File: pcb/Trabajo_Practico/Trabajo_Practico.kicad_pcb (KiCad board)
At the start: 2 copper layers, 72.5 x 56 mm, 13 parts, among them J1 Conn_02x19_Odd_Even, J2 Conn_02x19_Odd_Even, J3 Conn_01x03_Male, J4 Conn_01x03_Male, U1 ESP8266-01_ESP-01, U2 MAX30102_P, U3 SD_Card_P, U4 DS18B20

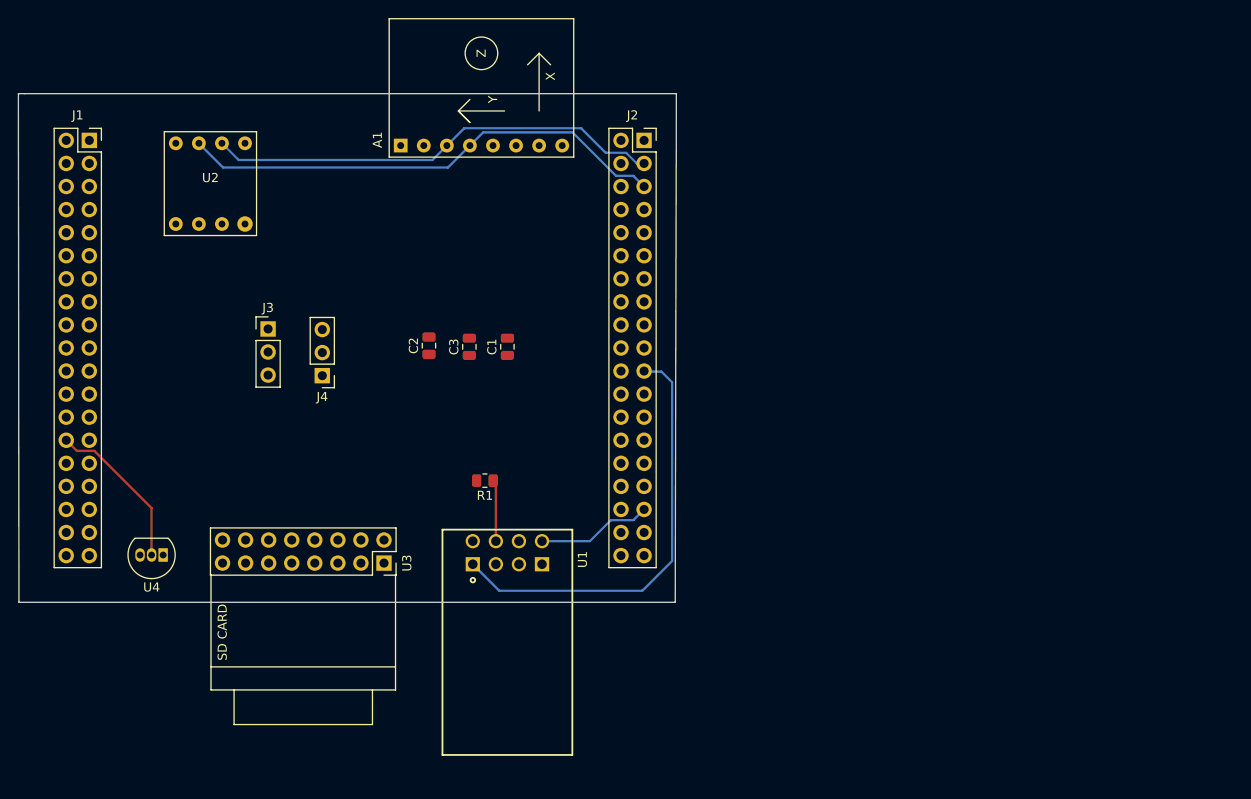
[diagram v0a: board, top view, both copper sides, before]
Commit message: Se ordena los componentes en el pcb
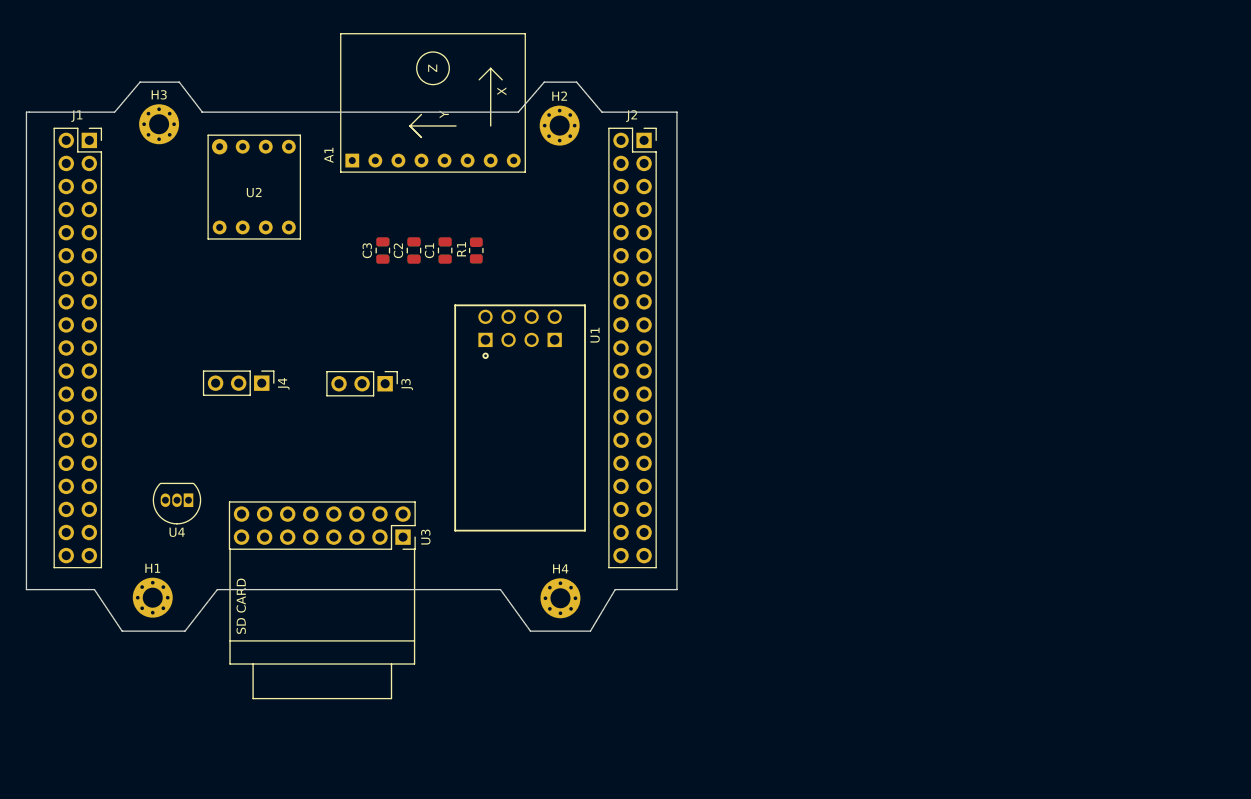
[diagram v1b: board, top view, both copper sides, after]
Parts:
- added H1: MountingHole, MountingHole:MountingHole_2.2mm_M2_Pad_Via, F.Cu at (53.4, 102.5)
- added H2: MountingHole, MountingHole:MountingHole_2.2mm_M2_Pad_Via, F.Cu at (98.2, 50.5)
- added H3: MountingHole, MountingHole:MountingHole_2.2mm_M2_Pad_Via, F.Cu at (54.1, 50.4)
- added H4: MountingHole, MountingHole:MountingHole_2.2mm_M2_Pad_Via, F.Cu at (98.3, 102.6)
- moved R1 25.4 mm to (89.0, 64.3), turned to 270 degrees
- moved U1 24.7 mm to (93.9, 74.1)
- moved C3 14.3 mm to (78.7, 64.3)
- moved J3 14.2 mm to (79.0, 78.9), turned to 270 degrees
- moved C1 12.6 mm to (85.6, 64.3)
- moved C2 10.6 mm to (82.2, 64.3)
- moved U2 8.81 mm to (63.3, 52.8), turned to 0 degrees
- moved J4 6.72 mm to (65.4, 78.9), turned to 270 degrees
- moved U4 6.65 mm to (57.3, 91.8)
- moved A1 5.58 mm to (75.4, 54.4)
- moved U3 3.54 mm to (81.0, 95.8)
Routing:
- net /PB9: track 54.2 -> 0.00 mm
- net /PB8: track 50.3 -> 0.00 mm
- net /PA9: track 47.8 -> 0.09 mm
- net /AN0: track 17.7 -> 0.00 mm
- net /PA10: track 12.7 -> 0.00 mm
- net Net-(R1-Pad1): track 6.79 -> 0.00 mm
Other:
- board size 72.5 x 56 mm -> 71.6 x 60.5 mm

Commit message: Se realizaron las correcciones
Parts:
- U4: footprint Package_TO_SOT_THT:TO-92_Inline -> Connector_PinHeader_2.54mm:PinHeader_1x03_P2.54mm_Vertical
- moved R1 37.9 mm to (54.0, 78.7), turned to 0 degrees
- moved C2 34.5 mm to (54.2, 84.5), turned to 180 degrees
- moved C1 30.1 mm to (59.2, 78.7), turned to 0 degrees
- moved C3 28.0 mm to (59.3, 84.5), turned to 0 degrees
- moved J3 26.3 mm to (99.6, 95.2)
- moved U4 18.8 mm to (72.2, 80.2), turned to 90 degrees
- moved J4 17.7 mm to (58.7, 95.2)
- moved A1 15.4 mm to (65.9, 66.5)
- moved U2 10.6 mm to (55.6, 60.0)
- moved J5 4.02 mm to (84.3, 93.5)
- moved U1 3.30 mm to (93.8, 77.4), turned to 90 degrees
- renumbered U3 to J5
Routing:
- net VCC: track 0.00 -> 110.6 mm
- net /PB8: track 0.00 -> 61.0 mm
- net /PB9: track 0.00 -> 57.6 mm
- net /CLK: track 0.00 -> 44.6 mm
- net Net-(R1-Pad1): track 0.00 -> 44.5 mm
- net /CS: track 0.00 -> 40.6 mm
- net /MOSI: track 0.00 -> 33.9 mm
- net /MISO: track 0.00 -> 33.0 mm
- net /AN0: track 0.00 -> 32.9 mm
- net /PA10: track 0.00 -> 31.4 mm
- net /PA9: track 0.09 -> 11.2 mm
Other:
- outline, holes or cut-outs redrawn
- rule via_min_drill: 0.3 -> 0.4
- rule via_min_size: 0.4 -> 0.5

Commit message: Presentacion final del proyecto
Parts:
- added C4: 100nF, Capacitor_SMD:C_0805_2012Metric, F.Cu at (116.3, 83.2)
- added D1: LED, LED_SMD:LED_0805_2012Metric_Pad1.15x1.40mm_HandSolder, F.Cu at (160.3, 101.0)
- added FID1: Fiducial, Fiducial:Fiducial_0.5mm_Mask1mm, F.Cu at (120.4, 63.6)
- added FID2: Fiducial, Fiducial:Fiducial_0.5mm_Mask1mm, F.Cu at (151.1, 63.6)
- added FID3: Fiducial, Fiducial:Fiducial_0.5mm_Mask1mm, F.Cu at (120.3, 103.0)
- added FID4: Fiducial, Fiducial:Fiducial_0.5mm_Mask1mm, F.Cu at (151.1, 102.9)
- added R2: 330, Resistor_SMD:R_0805_2012Metric, F.Cu at (155.7, 101.0)
- moved R1 104.6 mm to (157.4, 94.8)
- moved U2 83.4 mm to (131.6, 94.4), turned to 180 degrees
- moved C2 62.3 mm to (116.3, 90.2)
- moved H2 62.2 mm to (159.4, 61.8)
- moved J2 62.2 mm to (168.7, 63.4)
- moved J3 62.2 mm to (160.8, 106.6)
- moved H1 62.2 mm to (114.6, 113.8)
- moved H3 62.2 mm to (115.3, 61.7)
- moved J4 62.2 mm to (119.9, 106.6)
- moved A1 62.2 mm to (127.1, 77.9)
- moved H4 62.2 mm to (159.5, 113.9)
- moved J5 62.2 mm to (145.5, 104.8)
- moved U1 62.2 mm to (155.0, 88.7)
- moved J1 62.2 mm to (107.6, 63.4)
- moved C1 58.9 mm to (116.3, 93.7), turned to 180 degrees
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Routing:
- net Net-(R1-Pad1): track 44.5 -> 3.65 mm
- net VCC: track 110.6 -> 151.1 mm
- net /PB8: track 61.0 -> 49.2 mm
- net /AN0: track 32.9 -> 28.7 mm
- net Net-(D1-Pad2): track 0.00 -> 2.67 mm
- net /PB9: track 57.6 -> 55.5 mm
- net /PA10: track 31.4 -> 32.1 mm
- net /CS: track 40.6 -> 41.2 mm
- net /MISO: track 33.0 -> 33.5 mm
- added copper zone on B.Cu, net GND
- added copper zone on F.Cu, net GND
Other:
- board text added: "16/08/21"
- board text added: "GND"
- board text added: "Ing. William's Limonchi FIUBA"
- board text added: "LED ON"
- board text added: "LIMA - PERÚ"
- board text added: "Módulo Detector de Caídas para núcelo STM32 v1.0"
- board text added: "Tamaño de placa * 72 mm * 61 mm Grilla: * 1 mm * 0.25 mm posicionamiento de componentes Tamaños: * 0.25 y 0.5 mm ancho de pista * 0.8 mm pad de vía * 0.5 mm agujero de vía Capas: Top: F.Cu Bottom: B.Cu"
- board text added: "VCC"
